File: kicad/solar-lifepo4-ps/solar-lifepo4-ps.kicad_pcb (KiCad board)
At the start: 2 copper layers, 65.5 x 40.5 mm, 29 parts, among them J1 Screw_Terminal_01x02, T1 SI4435DY, U1 CN3722

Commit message: still WIP
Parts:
- added BAT1: ~, foxisfrickellibrary:batteryholder_keystone_1106, F.Cu at (88.0, 113.5)
- added C11: 100nF, Capacitor_SMD:C_0402_1005Metric, F.Cu at (125.0, 69.5)
- added R11: 100, Resistor_SMD:R_0805_2012Metric, F.Cu at (125.0, 72.5)
- added R2: 1.8k, Resistor_SMD:R_0603_1608Metric, F.Cu at (116.5, 73.5)
- added T2: AO3400A, Package_TO_SOT_SMD:SOT-23, F.Cu at (112.5, 68.0)
- added T3: AO3400A, Package_TO_SOT_SMD:SOT-23, F.Cu at (112.5, 73.0)
- added U2: HY2112, Package_TO_SOT_SMD:SOT-23-6, F.Cu at (120.5, 70.0)
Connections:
- net VBATCHG+ renamed VBAT+
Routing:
- net VBAT-: track 0.00 -> 20.5 mm
- net Net-(T3-G): track 0.00 -> 12.8 mm
- net Net-(T2-G): track 0.00 -> 7.26 mm
- net Net-(U2-VDD): track 0.00 -> 4.98 mm
- net Net-(U2-CS): track 0.00 -> 4.95 mm
- net GND: track 71.6 -> 74.8 mm
- net Net-(T2-D): track 0.00 -> 3.12 mm
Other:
- board size 65.5 x 40.5 mm -> 94 x 72 mm

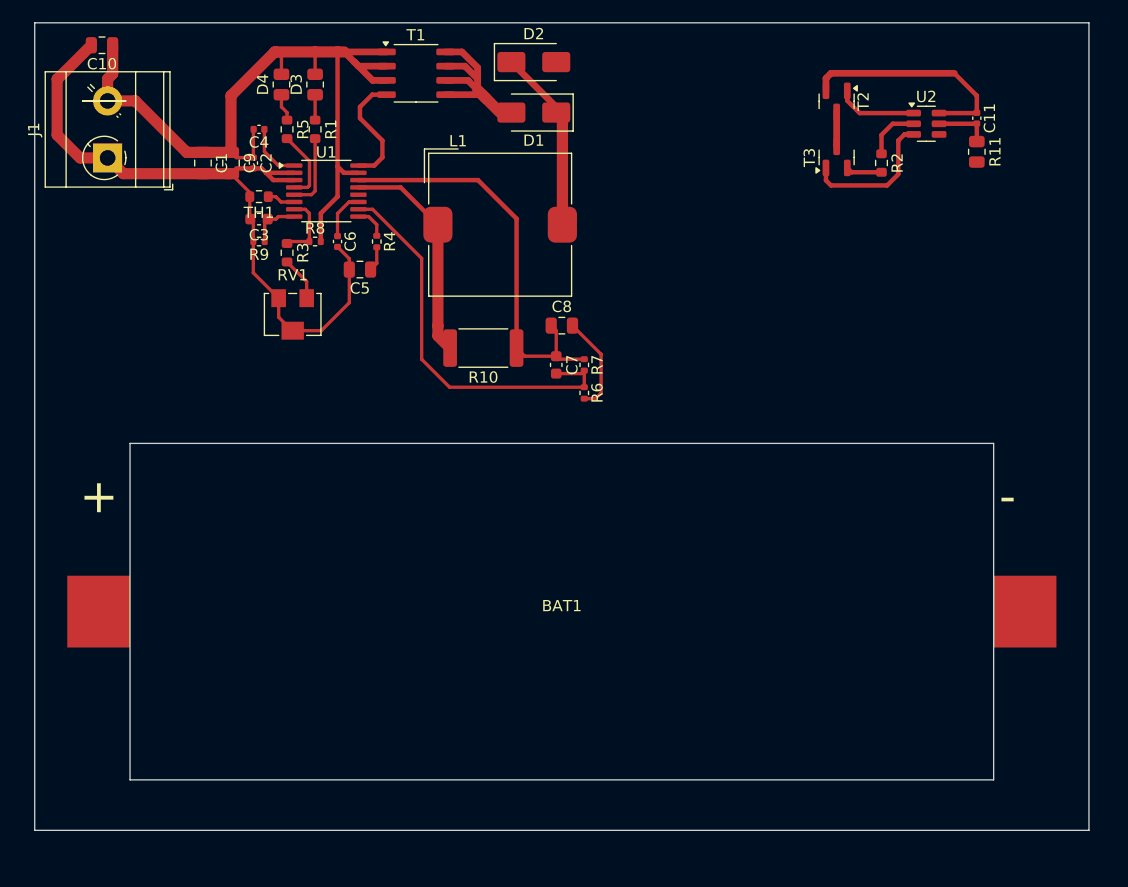
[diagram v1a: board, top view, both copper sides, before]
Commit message: current state. All the main circuit has been designed now. TODO: voltage divider output to permit a connected MC to measure voltages; fix square hole in PCB because JLCPCB will not be able to manufacture that, we need to round the edges.
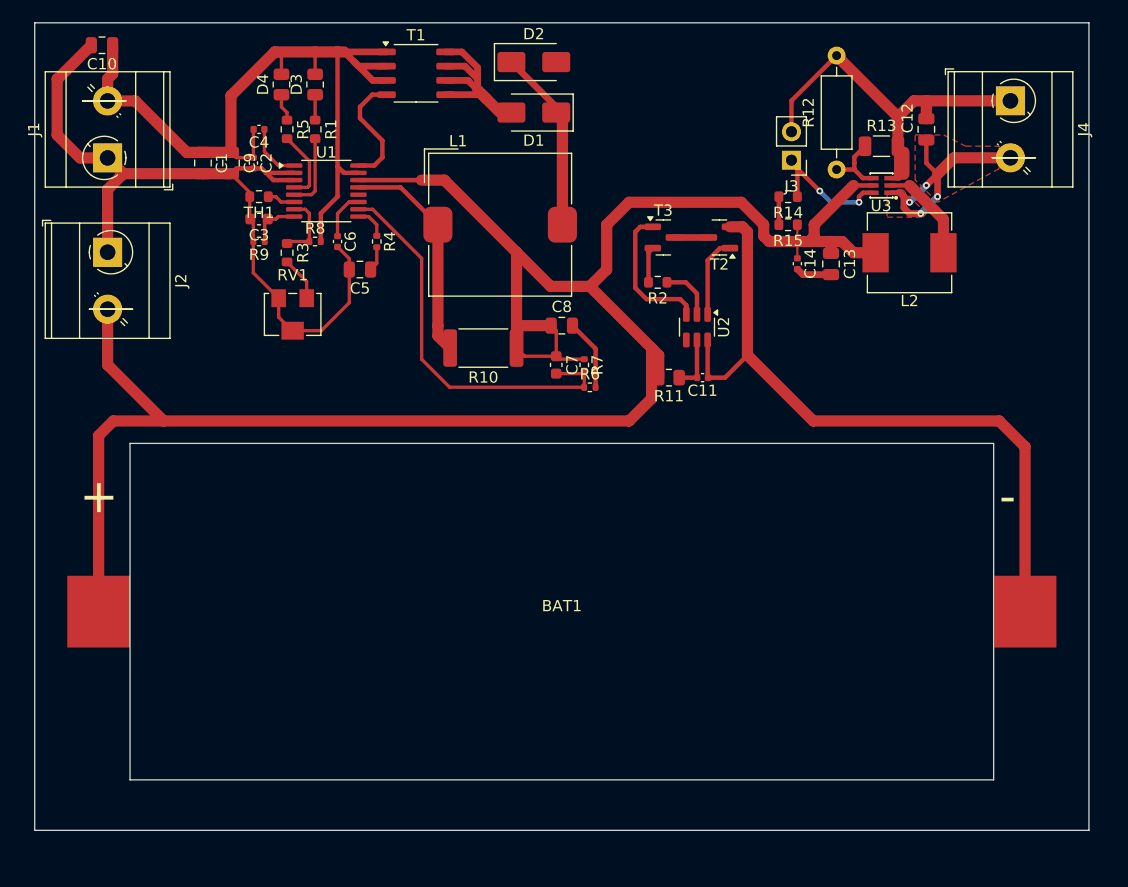
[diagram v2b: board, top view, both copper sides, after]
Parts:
- added C12: 22uF, Capacitor_SMD:C_0805_2012Metric, F.Cu at (120.5, 70.5)
- added C13: 22uF, Capacitor_SMD:C_0805_2012Metric, F.Cu at (112.0, 82.5)
- added C14: 100nF, Capacitor_SMD:C_0402_1005Metric, F.Cu at (109.0, 82.5)
- added J2: Screw_Terminal_01x02, TerminalBlock_MetzConnect:TerminalBlock_MetzConnect_Type073_RT02602HBLU_1x02_P5.08mm_Horizontal, F.Cu at (47.5, 81.5)
- added J3: disable-Jumper, Connector_PinHeader_2.54mm:PinHeader_1x02_P2.54mm_Vertical, F.Cu at (108.5, 73.2)
- added J4: Screw_Terminal_01x02, TerminalBlock_MetzConnect:TerminalBlock_MetzConnect_Type073_RT02602HBLU_1x02_P5.08mm_Horizontal, F.Cu at (128.0, 68.0)
- added L2: 4.7uH, Inductor_SMD:L_Sunlord_MWSA0603S, F.Cu at (119.0, 81.5)
- added R12: VoltageSelA, Resistor_THT:R_Axial_DIN0207_L6.3mm_D2.5mm_P10.16mm_Horizontal, F.Cu at (112.5, 74.1)
- added R13: VoltageSelB, Resistor_SMD:R_1206_3216Metric, F.Cu at (116.5, 72.0)
- added R14: 10M, Resistor_SMD:R_0603_1608Metric, F.Cu at (108.2, 76.5)
- added R15: 10M, Resistor_SMD:R_0603_1608Metric, F.Cu at (108.2, 79.0)
- added U3: MAX17224ELT+T, foxisfrickellibrary:UDFN-6_L2.0-W2.0-P0.65-BL-1, F.Cu at (116.5, 75.5)
- moved R11 34.0 mm to (97.5, 92.6), turned to 180 degrees
- moved C11 33.7 mm to (100.5, 92.6), turned to 180 degrees
- moved U2 27.3 mm to (100.0, 88.1), turned to -90 degrees
- moved R2 22.6 mm to (96.5, 84.1), turned to 180 degrees
- moved T3 17.0 mm to (97.0, 80.1), turned to 0 degrees
- moved T2 16.0 mm to (102.0, 80.1), turned to 180 degrees
- moved R6 0.71 mm to (90.5, 93.5), turned to 0 degrees
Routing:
- net VBAT+: track 36.4 -> 185.0 mm
- net GND: track 74.8 -> 121.1 mm
- net VBAT-: track 20.5 -> 63.3 mm
- net VREGOUT: track 0.00 -> 23.0 mm, vias 0 -> 4
- net Net-(J3-Pin_1): track 0.00 -> 12.8 mm, vias 0 -> 2
- net Net-(U3-LX): track 0.00 -> 9.00 mm
- net Net-(U3-SEL): track 0.00 -> 6.05 mm
- net Net-(R14-Pad2): track 0.00 -> 2.50 mm
- added copper zone on F.Cu, net VREGOUT

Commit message: rev 0, as it was sent to jlcpcb for production.
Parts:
- added C15: 1nF, Capacitor_SMD:C_0603_1608Metric, F.Cu at (56.5, 91.0)
- added C16: 1nF, Capacitor_SMD:C_0603_1608Metric, F.Cu at (94.5, 64.5)
- added J5: SenseVBAT, Connector_PinHeader_2.54mm:PinHeader_1x01_P2.54mm_Vertical, F.Cu at (98.5, 67.5)
- added J6: SenseVSOLAR, Connector_PinHeader_2.54mm:PinHeader_1x01_P2.54mm_Vertical, F.Cu at (57.0, 85.5)
- added R16: 10M, Resistor_SMD:R_0603_1608Metric, F.Cu at (95.5, 72.0)
- added R17: 10M, Resistor_SMD:R_0603_1608Metric, F.Cu at (94.5, 67.0)
- added R18: 1M, Resistor_SMD:R_0402_1005Metric, F.Cu at (56.5, 89.0)
- added R19: 10M, Resistor_SMD:R_0603_1608Metric, F.Cu at (56.0, 80.5)
- BAT1: footprint foxisfrickellibrary:batteryholder_keystone_1106 -> foxisfrickellibrary:batteryholder_keystone_1106-jlcpcb
- moved BAT1 1.50 mm to (88.0, 112.0)
- renumbered J4 to J3, J3 to J4
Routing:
- net GND: track 121.1 -> 245.8 mm, vias 0 -> 12
- net Net-(J6-Pin_1): track 0.00 -> 10.6 mm
- net VSOLAR+: track 75.0 -> 85.5 mm, vias 0 -> 2
- net Net-(J5-Pin_1): track 0.00 -> 10.2 mm
- net VBAT+: track 185.0 -> 189.3 mm
- net VBAT-: track 63.3 -> 66.4 mm
- added copper zone on B.Cu, net GND
- added copper zone on F.Cu, net GND
- added copper zone on F.Cu, net Net-(D1-A)
- added copper zone on F.Cu, net VBAT+
- added copper zone on F.Cu, net VBAT-
- added copper zone on F.Cu, net VSOLAR+
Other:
- board size 94 x 72 mm -> 94 x 75 mm
- board text added: "26650 LiFePO4 cell"
- board text added: "Battery OUT"
- board text added: "JLCJLCJLCJLC"
- board text added: "MPPT Adjust"
- board text added: "PoempelFox Solar LiFePO4 PowerSupply"
- board text added: "Rev. 0"
- board text added: "Solar IN"
- board text added: "VBatMeas"
- board text added: "VReg OUT"
- board text added: "VSolMeas"
- board text added: "Voltage set to:"
- board text added: "disable VReg →"

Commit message: first few fixes after Rev. 0 arrived from the JLCPCB-fab. It seems to be mostly working fine, but I made a few small errors - like forgetting the labels for +/- and using resistor-footprints for the two LEDs
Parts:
- D3, D4: footprint Resistor_SMD:R_0805_2012Metric -> LED_SMD:LED_0805_2012Metric
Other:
- board text added: "+"
- board text added: "-"
- board text added: "Rev. 1"
- board text added: "disable VReg"
- board text removed: "Rev. 0"
- board text removed: "disable VReg →"

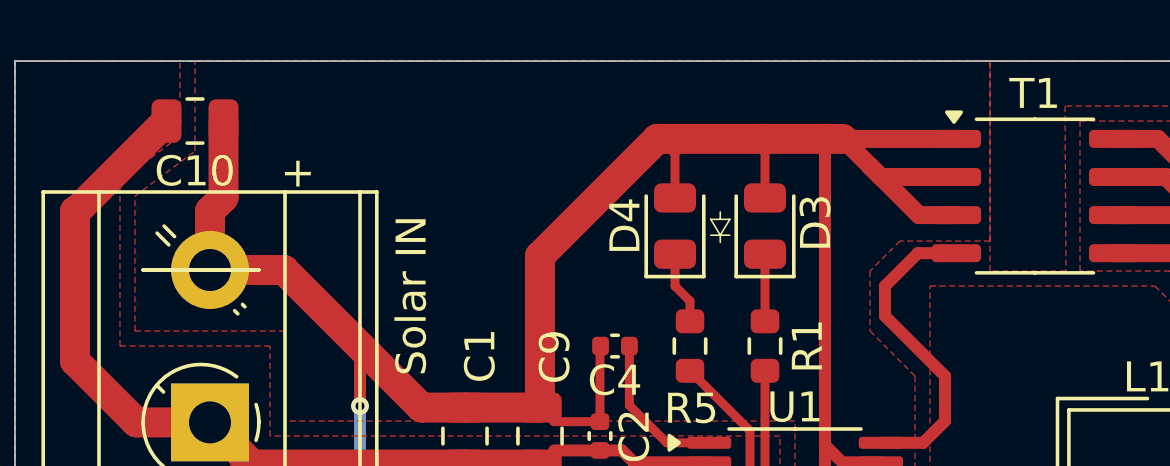
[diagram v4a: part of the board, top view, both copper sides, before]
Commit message: more labeling on the silkscreen, minor ground plane movement.
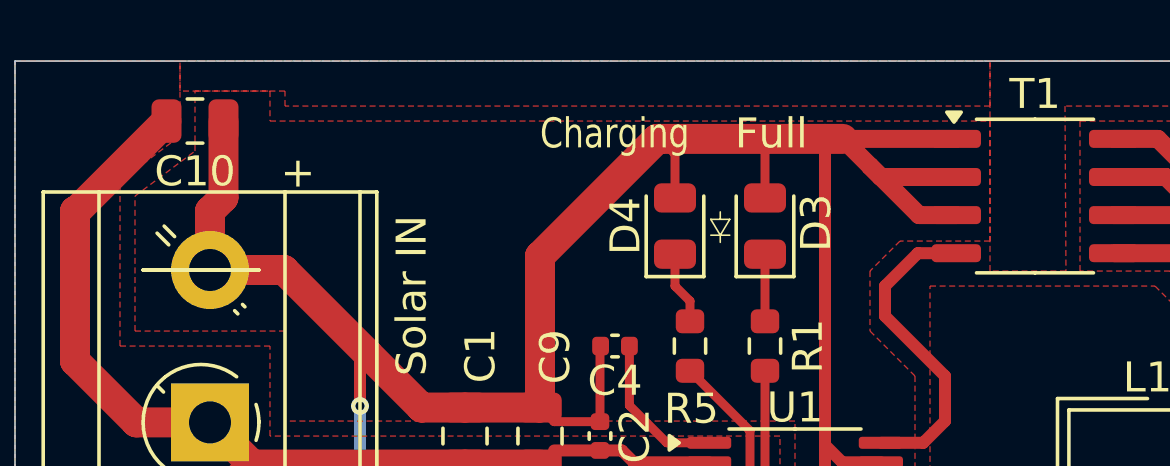
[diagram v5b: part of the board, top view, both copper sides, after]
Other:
- board text added: "* can be exceeded when VBat is high and Load is low"
- board text added: "Charging"
- board text added: "Full"
- board text added: "R (kΩ) 80.6 66.5 0.0"
- board text added: "Vout 3.3* 3.4 5.0"
- board text added: "maxI (mA) ~600 ~600 ~400"
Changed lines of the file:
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@@
 	)
 	(gr_line
+		(start 134 93.5)
+		(end 114 93.5)
+		(stroke
+			(width 0.1)
+			(type default)
+		)
+		(layer "B.SilkS")
+	)
+	(gr_line
+		(start 114 90.5)
+		(end 134 90.5)
+		(stroke
+			(width 0.1)
+			(type default)
+		)
+		(layer "B.SilkS")
+	)
+	(gr_line
+		(start 127.5 93.5)
+		(end 127.5 87)
+		(stroke
+			(width 0.1)
+			(type default)
+		)
+		(layer "B.SilkS")
+	)
+	(gr_line
+		(start 114 93.5)
+		(end 114 87)
+		(stroke
+			(width 0.1)
+			(type default)
+		)
+		(layer "B.SilkS")
+	)
+	(gr_line
+		(start 134 87)
+		(end 134 93.5)
+		(stroke
+			(width 0.1)
+			(type default)
+		)
+		(layer "B.SilkS")
+	)
+	(gr_line
+		(start 114 87)
+		(end 134 87)
+		(stroke
+			(width 0.1)
+			(type default)
+		)
+		(layer "B.SilkS")
+	)
+	(gr_line
+		(start 134 92)
+		(end 114 92)
+		(stroke
+			(width 0.1)
+			(type default)
+		)
+		(layer "B.SilkS")
+	)
+	(gr_line
+		(start 114 89)
+		(end 134 89)
+		(stroke
+			(width 0.1)
+			(type default)
+		)
+		(layer "B.SilkS")
+	)
+	(gr_line
+		(start 122.5 93.5)
+		(end 122.5 87)
+		(stroke
+			(width 0.1)
+			(type default)
+		)
+		(layer "B.SilkS")
+	)
+	(gr_line
 		(start 64.826948 66.275809)
 		(end 64.191948 66.275809)
@@
 		(layer "Edge.Cuts")
 	)
+	(gr_text "* can be exceeded when\n  VBat is high and Load\n  is low"
+		(at 113 93 -0)
+		(layer "B.SilkS")
+		(effects
+			(font
+				(size 1 1)
+				(thickness 0.15)
+			)
+			(justify left bottom mirror)
+		)
+	)
+	(gr_text "R (kΩ)\n80.6\n66.5\n0.0"
+		(at 128.5 93.5 -0)
+		(layer "B.SilkS")
+		(effects
+			(font
+				(size 1 1)
+				(thickness 0.15)
+			)
+			(justify right bottom mirror)
+		)
+	)
 	(gr_text "+"
 		(at 133 73 90)
@@
 		)
 	)
+	(gr_text "Vout\n3.3*\n3.4\n5.0"
+		(at 125 93.5 -0)
+		(layer "B.SilkS")
+		(effects
+			(font
+				(size 1 1)
+				(thickness 0.15)
+			)
+			(justify bottom mirror)
+		)
+	)
+	(gr_text "maxI (mA)\n~600\n~600\n~400"
+		(at 118.5 93.5 -0)
+		(layer "B.SilkS")
+		(effects
+			(font
+				(size 1 1)
+				(thickness 0.15)
+			)
+			(justify bottom mirror)
+		)
+	)
 	(gr_text "-"
 		(at 43.5 80.5 90)
@@
 		)
 	)
+	(gr_text "Charging"
+		(at 58.5 64 0)
+		(layer "F.SilkS")
+		(effects
+			(font
+				(size 1 0.8)
+				(thickness 0.15)
+			)
+			(justify left bottom)
+		)
+	)
 	(gr_text "PoempelFox Solar LiFePO4 PowerSupply"
 		(at 56.5 133 0)
@@
 		)
 	)
+	(gr_text "Full"
+		(at 65 64 0)
+		(layer "F.SilkS")
+		(effects
+			(font
+				(size 1 1)
+				(thickness 0.15)
+			)
+			(justify left bottom)
+		)
+	)
 	(gr_text "-"
 		(at 50.983309 78.826877 90)
@@
 		)
 	)
-	(gr_text_box "R12/R13 set output voltage (populate only one of them!) between 3.4 and 5.0V."
-		(start 114.25 87)
-		(end 133.75 91.5)
-		(layer "F.SilkS")
+	(gr_text_box "R12/R13 set the output voltage (populate only one of them!) between 3.4 and 5.0V."
+		(start 113.25 86.5)
+		(end 134.25 79.5)
+		(layer "B.SilkS")
 		(effects
 			(font
-				(size 0.8 0.8)
+				(size 1 1)
 				(thickness 0.15)
 			)
-			(justify right top)
+			(justify left top mirror)
 		)
-		(border yes)
+		(border no)
 		(stroke
 			(width 0.1)
@@
 	)
 	(zone
+		(net 3)
+		(net_name "GND")
+		(layer "F.Cu")
+		(hatch edge 0.5)
+		(priority 15)
+		(connect_pads
+			(clearance 0.2)
+		)
+		(min_thickness 0.25)
+		(filled_areas_thickness no)
+		(fill yes
+			(thermal_gap 0.5)
+			(thermal_bridge_width 0.5)
+		)
+		(polygon
+			(pts
+				(xy 73.5 61) (xy 73.5 62.5) (xy 50 62.5) (xy 50 62) (xy 46.5 62) (xy 46.5 61)
+			)
+		)
+	)
+	(zone
 		(net 1)
 		(net_name "Net-(D1-A)")
@@
 		(polygon
 			(pts
-				(xy 45 70) (xy 45 65.5) (xy 47 64) (xy 47 61) (xy 73.5 61) (xy 73.5 67) (xy 70.5 67) (xy 69.5 68)
-				(xy 69.5 70) (xy 71 71.5) (xy 71 76.5) (xy 67 76.5) (xy 67 73) (xy 50 73) (xy 50 70)
+				(xy 45 70) (xy 45 65.5) (xy 47 64) (xy 47 62) (xy 49.5 62) (xy 49.5 63) (xy 73.5 63) (xy 73.5 67)
+				(xy 70.5 67) (xy 69.5 68) (xy 69.5 70) (xy 71 71.5) (xy 71 76.5) (xy 67 76.5) (xy 67 73) (xy 50 73)
+				(xy 50 70)
 			)
 		)
@@
 		)
 	)
+	(group ""
+		(members "189b546b-e713-47a1-84fd-97a1c59bf6a5" "29fb4339-fc79-46bb-9e1c-39739aea5712"
+			"3412053f-cbf6-4bfe-b230-4b5c103d5304" "3b68973f-2926-4d28-8a5a-c1568ee65b08"
+			"74e847b6-513e-492a-bd95-70ba3496d7c4" "7b393358-c17d-47a6-88af-df0cdd9d8c34"
+			"92974f51-8fed-41d1-8944-712b7344e4b7" "983de31e-365b-47d0-9421-1e649899f8fa"
+			"a2699e39-8f01-4877-a0d7-23b1a0034c15" "a4808ff7-5864-4fcf-948e-dc29ba60f7c6"
+			"ab9e8cad-386b-4b0d-a000-5a4edcd671d7" "b88cba2f-a83a-48e1-b705-1d13a09334f6"
+			"e45f1334-8018-44f1-8806-90b6124eff3a"
+		)
+	)
